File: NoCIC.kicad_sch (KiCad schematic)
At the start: 12 parts, among them J1 CIC, U1 74LVC1G06, U2 LMC555xM, U3 74LVC1G04

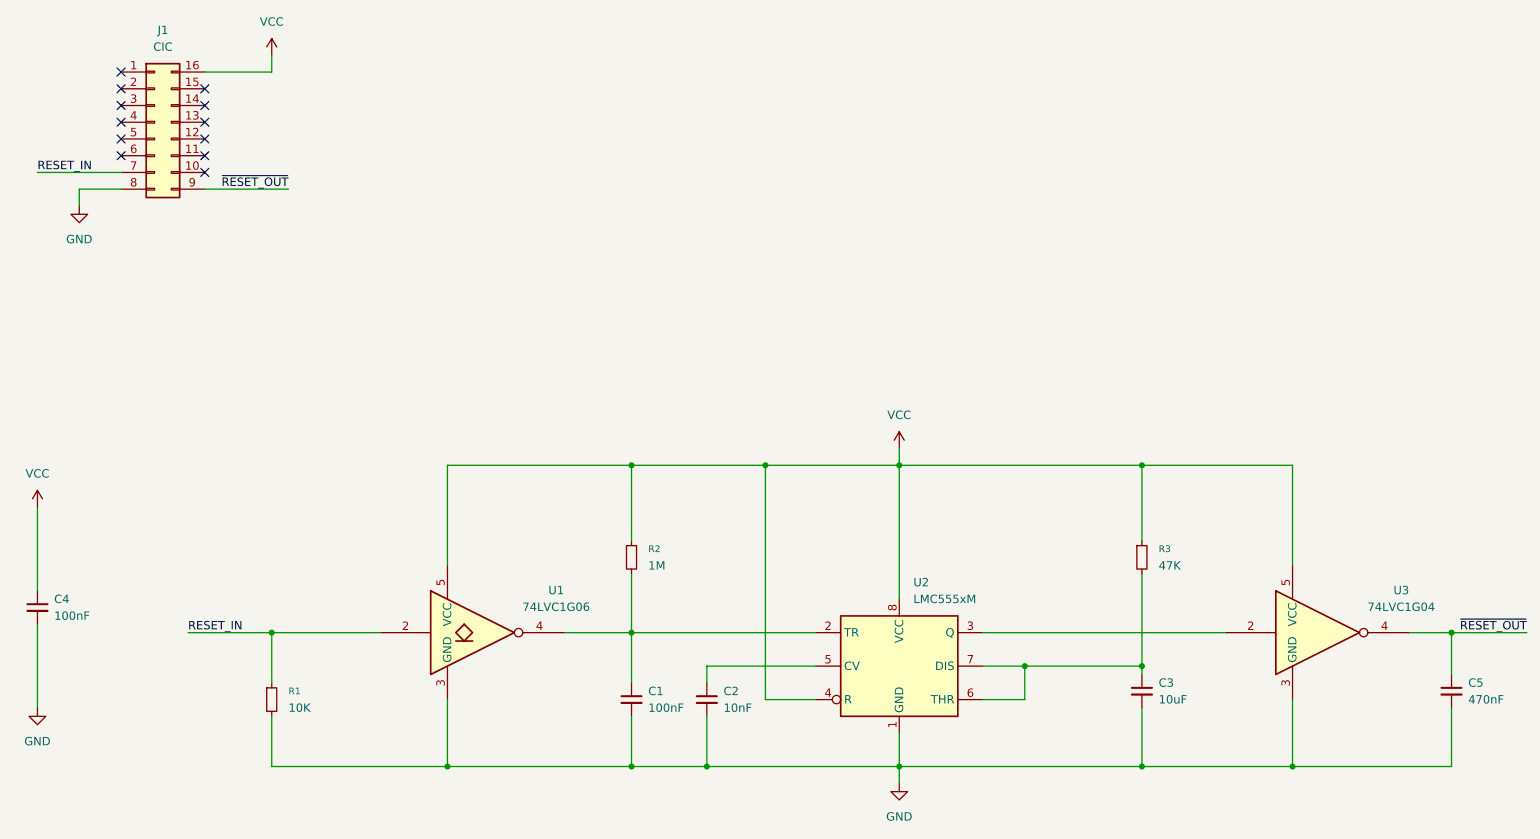
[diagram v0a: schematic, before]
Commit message: Add a jumper option to connect 555 output to pin 10, for CIC-RESET
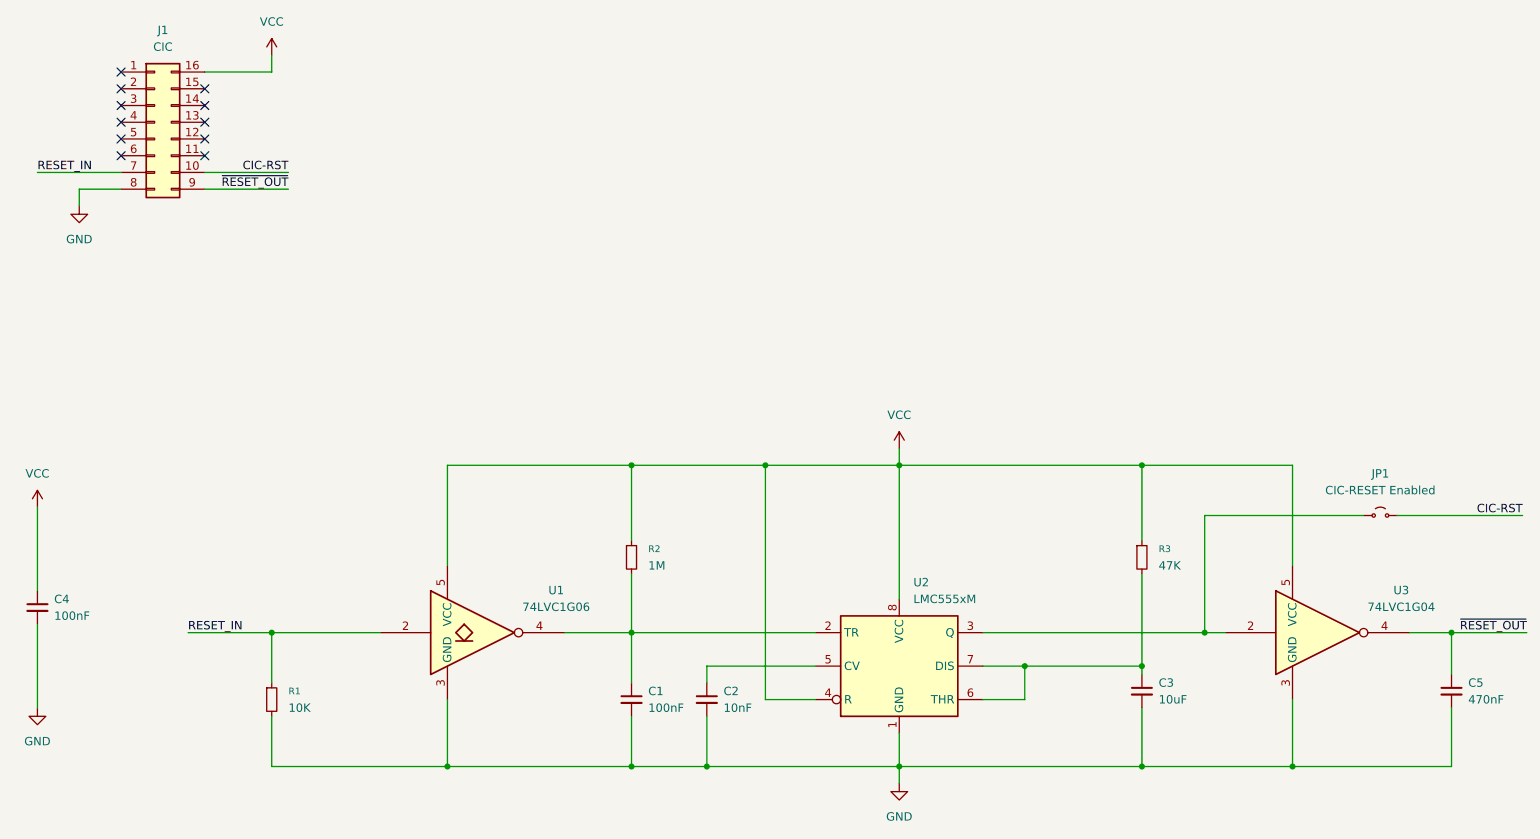
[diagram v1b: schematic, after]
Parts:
- added JP1: CIC-RESET Enabled, Jumper:SolderJumper-2_P1.3mm_Open_RoundedPad1.0x1.5mm, symbol Jumper:Jumper_2_Small_Open
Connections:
- net at U2.3 (Q), U3.2: now also JP1.1 (A)
- net CIC-RST: now reaches J1.10 (Pin_10)
- net CIC-RST: now also JP1.2 (B)
- no-connect marks 12 -> 11
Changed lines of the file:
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@@
+	)
+	(junction
+		(at 202.565 120.65)
+		(diameter 0)
+		(color 0 0 0 0)
 	)
 	(junction
@@
 	)
 	(no_connect
-		(at 50.8 50.8)
-	)
-	(no_connect
 		(at 50.8 45.72)
 	)
@@
 	(wire
 		(pts
+			(xy 226.695 102.87) (xy 202.565 102.87)
+		)
+		(stroke
+			(width 0)
+			(type default)
+		)
+	)
+	(wire
+		(pts
 			(xy 115.57 106.68) (xy 115.57 95.25)
 		)
@@
 	(wire
 		(pts
+			(xy 231.775 102.87) (xy 250.825 102.87)
+		)
+		(stroke
+			(width 0)
+			(type default)
+		)
+	)
+	(wire
+		(pts
 			(xy 193.04 140.97) (xy 193.04 132.08)
 		)
@@
 	(wire
 		(pts
+			(xy 50.8 50.8) (xy 63.5 50.8)
+		)
+		(stroke
+			(width 0)
+			(type default)
+		)
+	)
+	(wire
+		(pts
 			(xy 87.63 140.97) (xy 115.57 140.97)
 		)
@@
 	(wire
 		(pts
-			(xy 168.91 120.65) (xy 205.74 120.65)
+			(xy 168.91 120.65) (xy 202.565 120.65)
 		)
 		(stroke
@@
 	(wire
 		(pts
+			(xy 202.565 120.65) (xy 205.74 120.65)
+		)
+		(stroke
+			(width 0)
+			(type default)
+		)
+	)
+	(wire
+		(pts
 			(xy 31.75 53.34) (xy 38.1 53.34)
 		)
@@
 		(pts
 			(xy 156.21 135.89) (xy 156.21 140.97)
+		)
+		(stroke
+			(width 0)
+			(type default)
+		)
+	)
+	(wire
+		(pts
+			(xy 202.565 102.87) (xy 202.565 120.65)
 		)
 		(stroke
@@
 	(label "~{RESET_OUT}"
 		(at 251.46 120.65 180)
+		(effects
+			(font
+				(size 1.27 1.27)
+			)
+			(justify right bottom)
+		)
+	)
+	(label "CIC-RST"
+		(at 63.5 50.8 180)
+		(effects
+			(font
+				(size 1.27 1.27)
+			)
+			(justify right bottom)
+		)
+	)
+	(label "CIC-RST"
+		(at 250.825 102.87 180)
 		(effects
 			(font
@@
 					(unit 1)
 				)
+			)
+		)
+	)
+	(symbol
+		(lib_id "Jumper:Jumper_2_Small_Open")
+		(at 229.235 102.87 0)
+		(unit 1)
+		(exclude_from_sim no)
+		(in_bom yes)
+		(on_board yes)
+		(dnp no)
+		(fields_autoplaced yes)
+		(property "Reference" "JP1"
+			(at 229.235 96.52 0)
+			(effects
+				(font
+					(size 1.27 1.27)
+				)
+			)
+		)
+		(property "Value" "CIC-RESET Enabled"
+			(at 229.235 99.06 0)
+			(effects
+				(font
+					(size 1.27 1.27)
+				)
+			)
+		)
+		(property "Footprint" "Jumper:SolderJumper-2_P1.3mm_Open_RoundedPad1.0x1.5mm"
+			(at 229.235 102.87 0)
+			(effects
+				(font
+					(size 1.27 1.27)
+				)
+				(hide yes)
+			)
+		)
+		(property "Datasheet" "~"
+			(at 229.235 102.87 0)
+			(effects
+				(font
+					(size 1.27 1.27)
+				)
+				(hide yes)
+			)
+		)
+		(property "Description" "Jumper, 2-pole, small symbol, open"
+			(at 229.235 102.87 0)
+			(effects
+				(font
+					(size 1.27 1.27)
+				)
+				(hide yes)
+			)
+		)
+		(pin "1"
+		)
+		(pin "2"
+		)
+		(instances
+			(project ""
+				(path "/bc4110f2-4ee2-488e-820f-9ed5410de9d6"
+					(reference "JP1")
+					(unit 1)
+				)

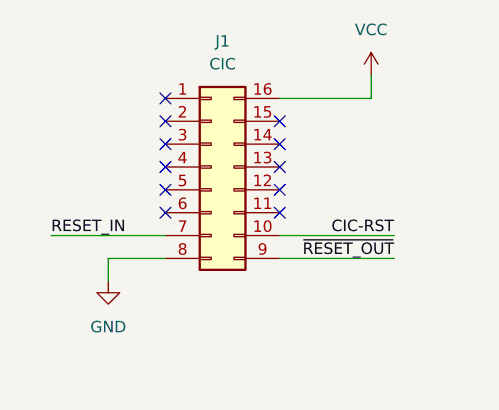
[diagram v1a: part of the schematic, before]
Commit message: Add load resistors on data lines
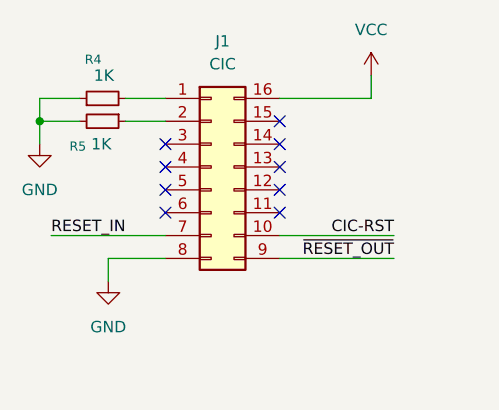
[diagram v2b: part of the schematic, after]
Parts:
- added R4, R5: 1K, Resistor_SMD:R_0805_2012Metric_Pad1.20x1.40mm_HandSolder, symbol Device:R_Small
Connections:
- net GND: now also R4.1, R5.2
- net at J1.1 (Pin_1): now also R4.2
- net at J1.2 (Pin_2): now also R5.1
- no-connect marks 11 -> 9
